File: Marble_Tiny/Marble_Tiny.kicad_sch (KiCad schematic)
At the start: 4 parts

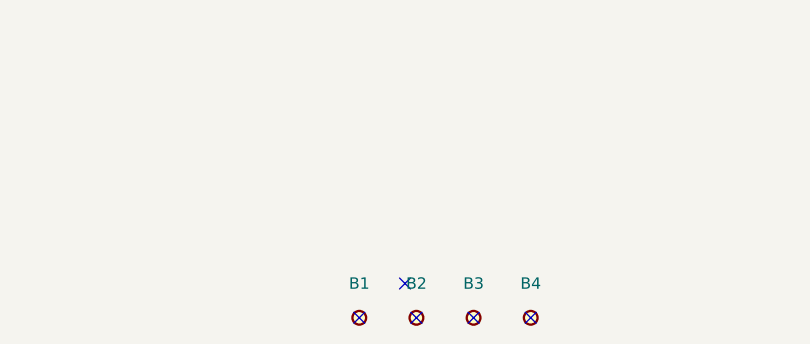
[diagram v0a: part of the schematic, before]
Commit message: connected more address lines to DDR, new board name
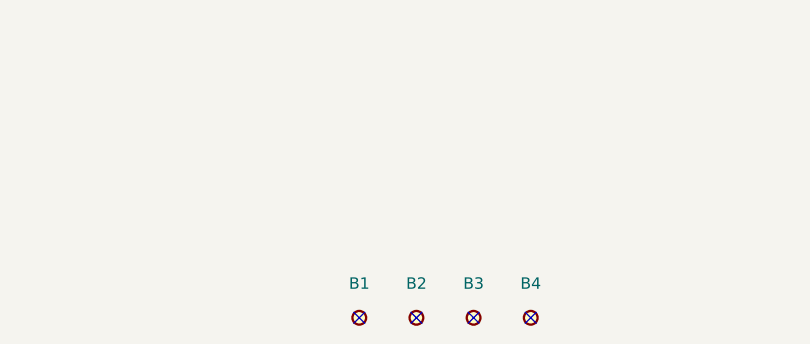
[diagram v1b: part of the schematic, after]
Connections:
- no-connect marks 5 -> 4
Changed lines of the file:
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@@
-	)
-	(no_connect
-		(at 163.83 241.3)
 	)
 	(no_connect
